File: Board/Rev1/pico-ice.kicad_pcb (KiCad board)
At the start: 4 copper layers, 22.9 x 61 mm, 99 parts, among them J1 USB_C_Receptacle_USB2.0, J2 Conn_02x20_Odd_Even, J3 Conn_02x20_Odd_Even, J4 PB_SEL, Q1 2N7002, SW1 PTS820 J25K SMTR LFS, SW2 PTS820 J25K SMTR LFS, U1 CL9293A12L5M, U2 W25Q32JVSSIQ, U3 RP2040, U4 CL9293A33L5M, U5 APS6404L-3SQN-SN, U6 ICE40UP5K-SG48ITR, U8 W25Q32JVSSIQ, Y1 12 MHz

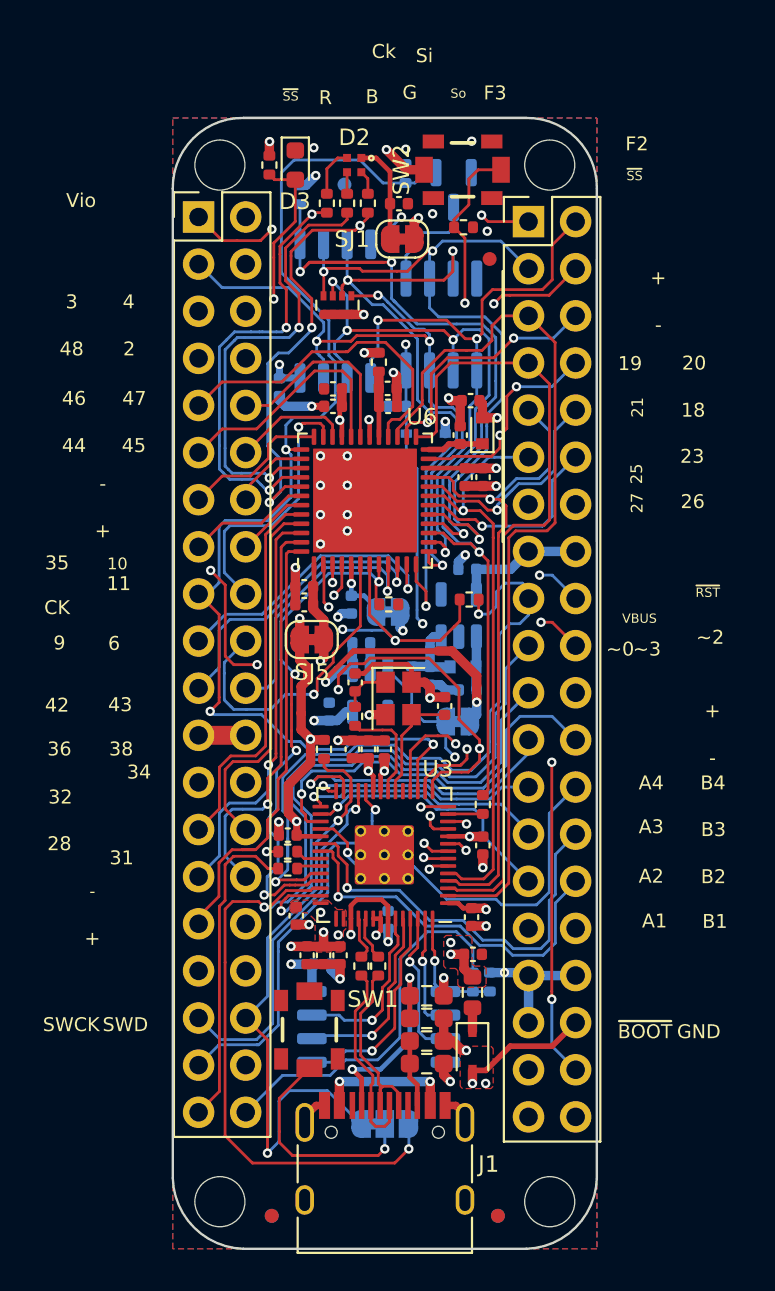
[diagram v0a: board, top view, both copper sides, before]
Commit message: Moved a few traces apart, esp on the clock related signals. Led to a couple of unwired signals.
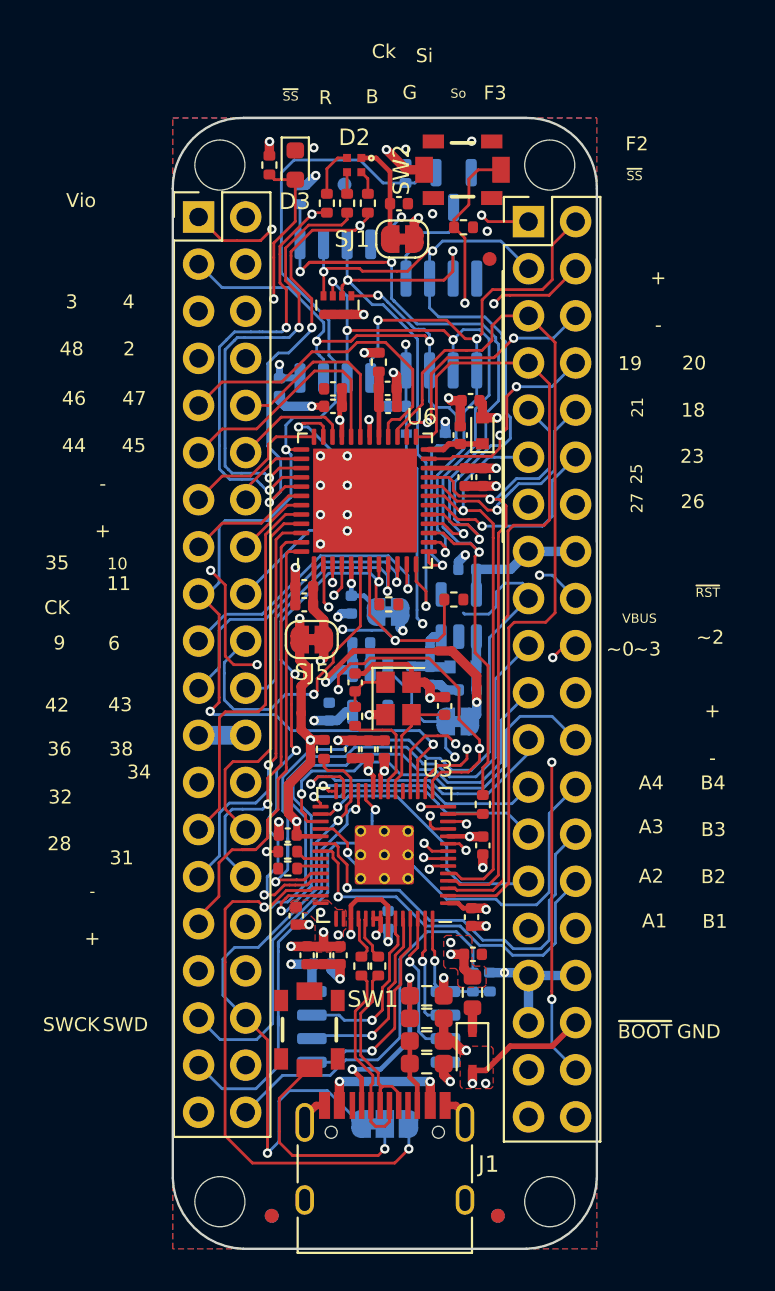
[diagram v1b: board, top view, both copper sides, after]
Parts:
- moved R25 0.83 mm to (76.1, 99.6)
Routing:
- net /SWCLK: track 21.3 -> 24.2 mm
- net /ICE_FLASH_IO2: track 45.5 -> 43.5 mm
- net /~{RESET}: track 33.6 -> 35.4 mm
- net /LED_R: track 73.3 -> 74.7 mm
- net /ICE_SI: track 60.1 -> 60.8 mm
- net /ICE_DONE_ADC0: track 37.4 -> 37.3 mm, vias 2 -> 1

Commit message: Update pico-ice.kicad_pcb
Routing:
- net /ICE_DONE_ADC0: track 37.3 -> 37.9 mm, vias 1 -> 2
- net /PICO_CLKOUT: track 16.9 -> 17.4 mm, vias 0 -> 1

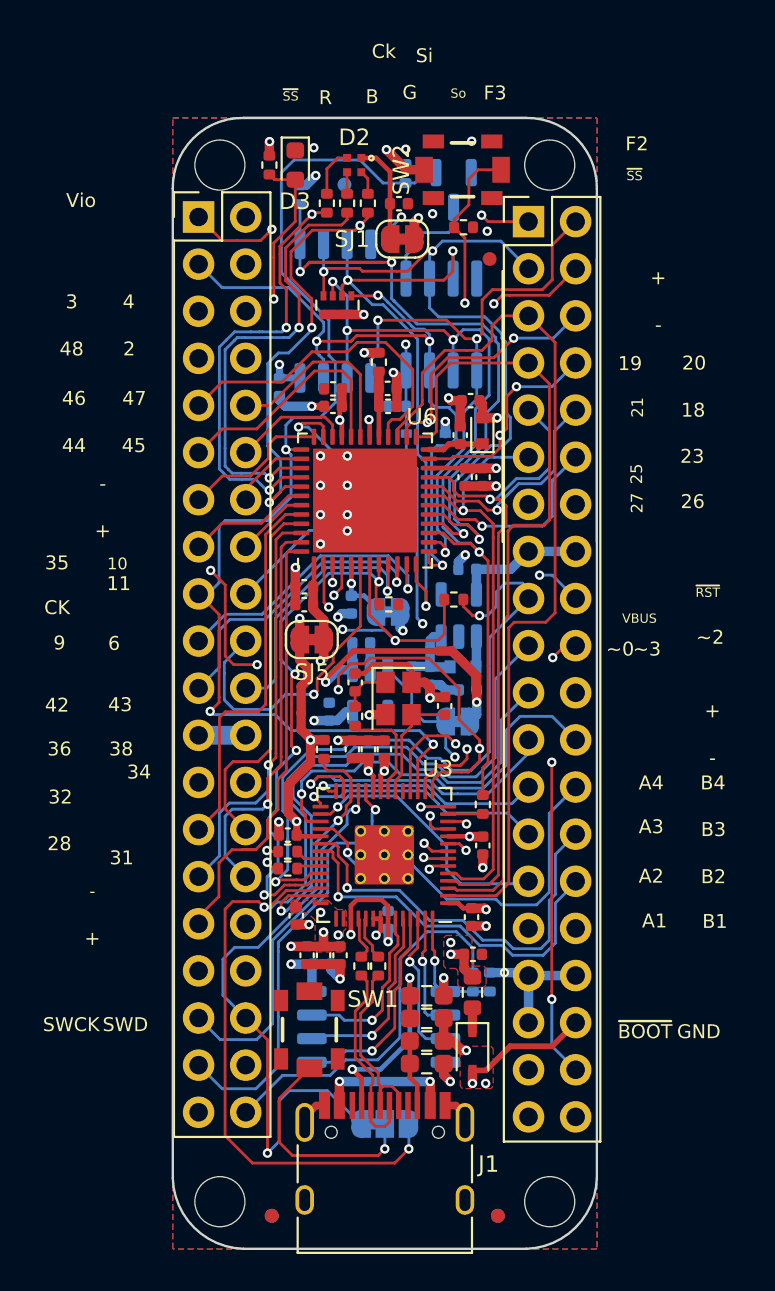
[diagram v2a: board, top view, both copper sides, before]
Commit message: Clean silkscreen
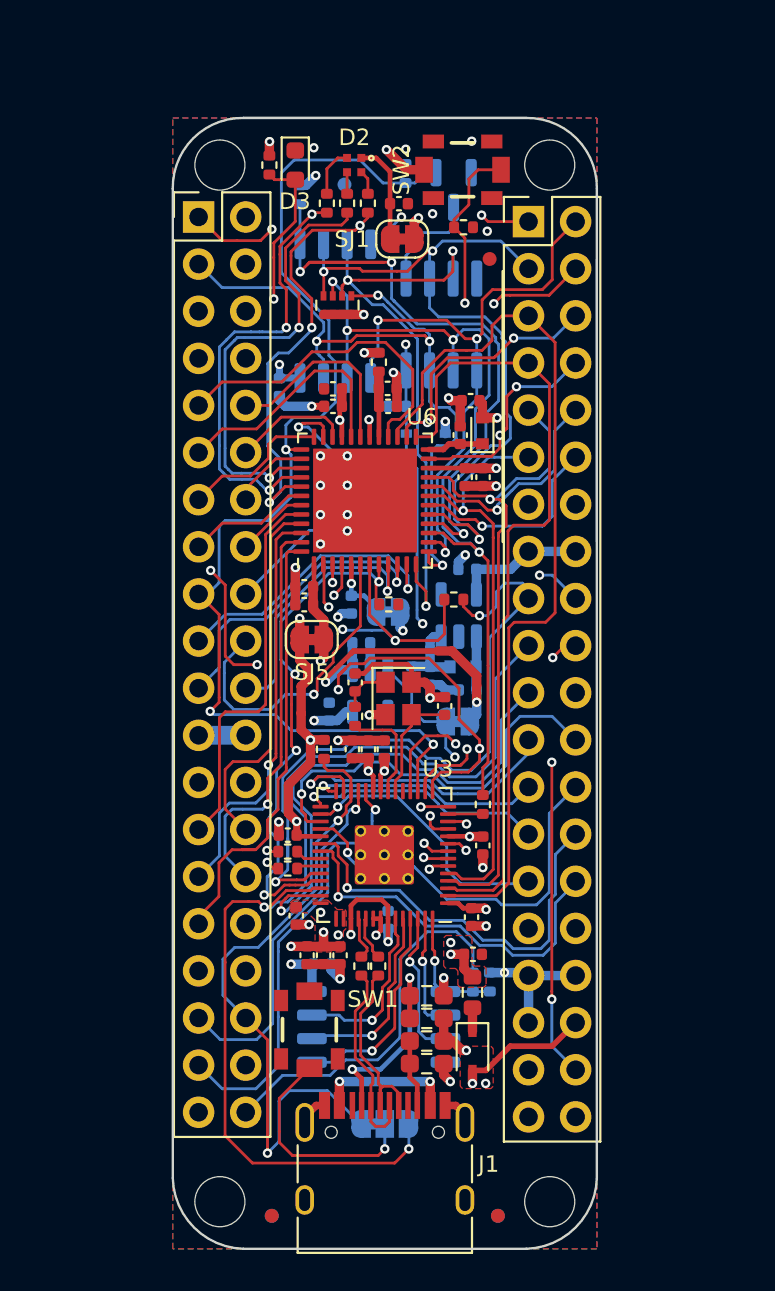
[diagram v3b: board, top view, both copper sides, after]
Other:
- board text removed: "+"
- board text removed: "-"
- board text removed: "10"
- board text removed: "11"
- board text removed: "18"
- board text removed: "19"
- board text removed: "2"
- board text removed: "20"
- board text removed: "21"
- board text removed: "23"
- board text removed: "25"
- board text removed: "26"
- board text removed: "27"
- board text removed: "28"
- board text removed: "3"
- board text removed: "31"
- board text removed: "32"
- board text removed: "34"
- board text removed: "35"
- board text removed: "36"
- board text removed: "38"
- board text removed: "4"
- board text removed: "42"
- board text removed: "43"
- board text removed: "44"
- board text removed: "45"
- board text removed: "46"
- board text removed: "47"
- board text removed: "48"
- board text removed: "6"
- board text removed: "9"
- board text removed: "A1"
- board text removed: "A2"
- board text removed: "A3"
- board text removed: "A4"
- board text removed: "B"
- board text removed: "B1"
- board text removed: "B2"
- board text removed: "B3"
- board text removed: "B4"
- board text removed: "CK"
- board text removed: "Ck"
- board text removed: "F2"
- board text removed: "F3"
- board text removed: "G"
- board text removed: "GND"
- board text removed: "R"
- board text removed: "RS"
- board text removed: "SWCK"
- board text removed: "SWD"
- board text removed: "Si"
- board text removed: "So"
- board text removed: "VBUS"
- board text removed: "Vio"
- board text removed: "~0"
- board text removed: "~2"
- board text removed: "~3"
- board text removed: "~{BOOT}"
- board text removed: "~{RST}"
- board text removed: "~{SS}"

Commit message: Update pico-ice.kicad_pcb
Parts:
- moved J2 1.02 mm to (62.2, 80.0)
- moved J3 0.77 mm to (80.0, 80.0)
- moved FID1 0.19 mm to (77.9, 81.3)
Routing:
- net /ICE_6: track 17.1 -> 12.6 mm
- net /ICE_4: track 29.8 -> 33.9 mm
- net /ICE_3: track 29.2 -> 33.2 mm
- net /LED_G: track 72.5 -> 70.0 mm
- net /PICO_PMOD_B3: track 22.2 -> 19.8 mm
- net /ICE_25: track 43.0 -> 41.0 mm
- net /~{ICE_RST}: track 53.2 -> 51.3 mm
- net /ICE_28: track 18.0 -> 19.7 mm
- net /ICE_35_G0: track 36.0 -> 37.6 mm
- net /LED_B: track 79.9 -> 78.2 mm
- net +3V3: track 60.3 -> 58.7 mm
- net /SRAM_SS: track 62.5 -> 64.1 mm
- net /ICE_27: track 48.2 -> 46.7 mm
- net /SWCLK: track 23.7 -> 22.3 mm
- net /ICE_SO: track 50.5 -> 49.2 mm
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
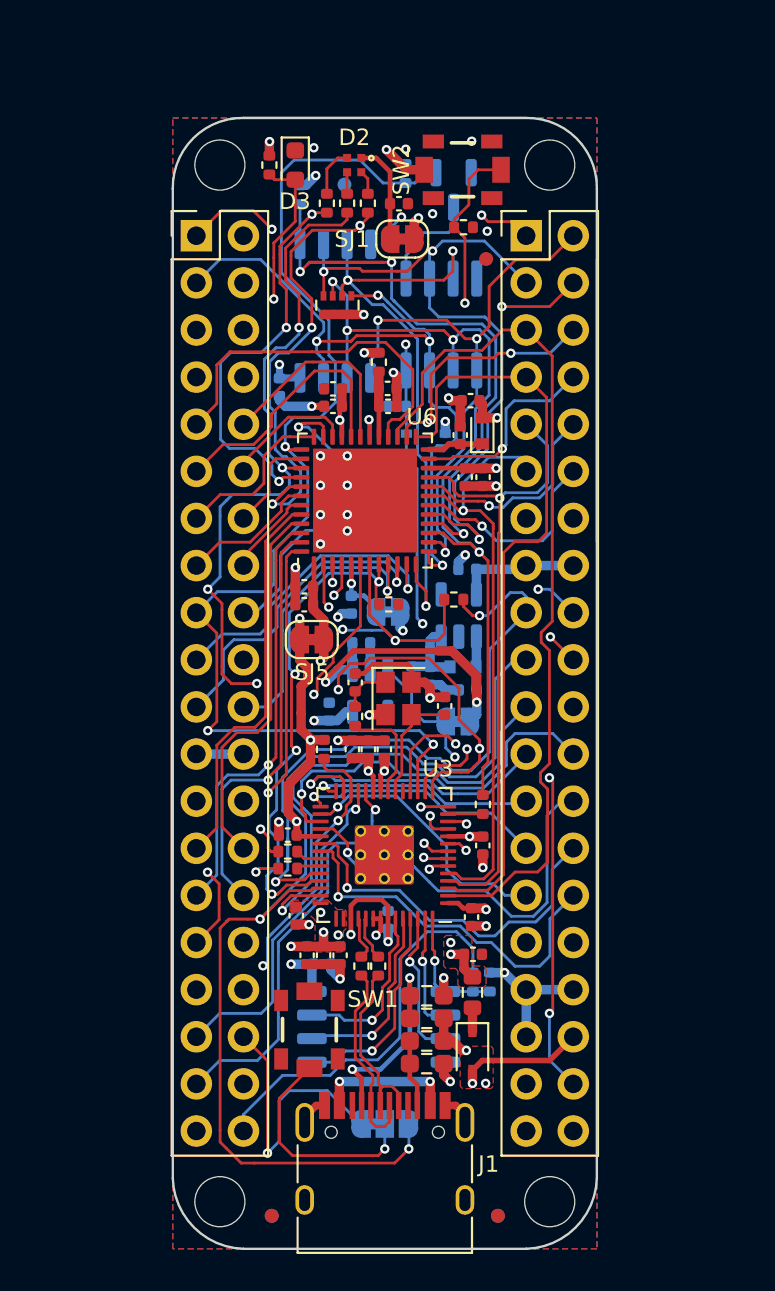
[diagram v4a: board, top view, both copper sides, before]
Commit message: Added silkscreen details, minor routing change to clear the logo
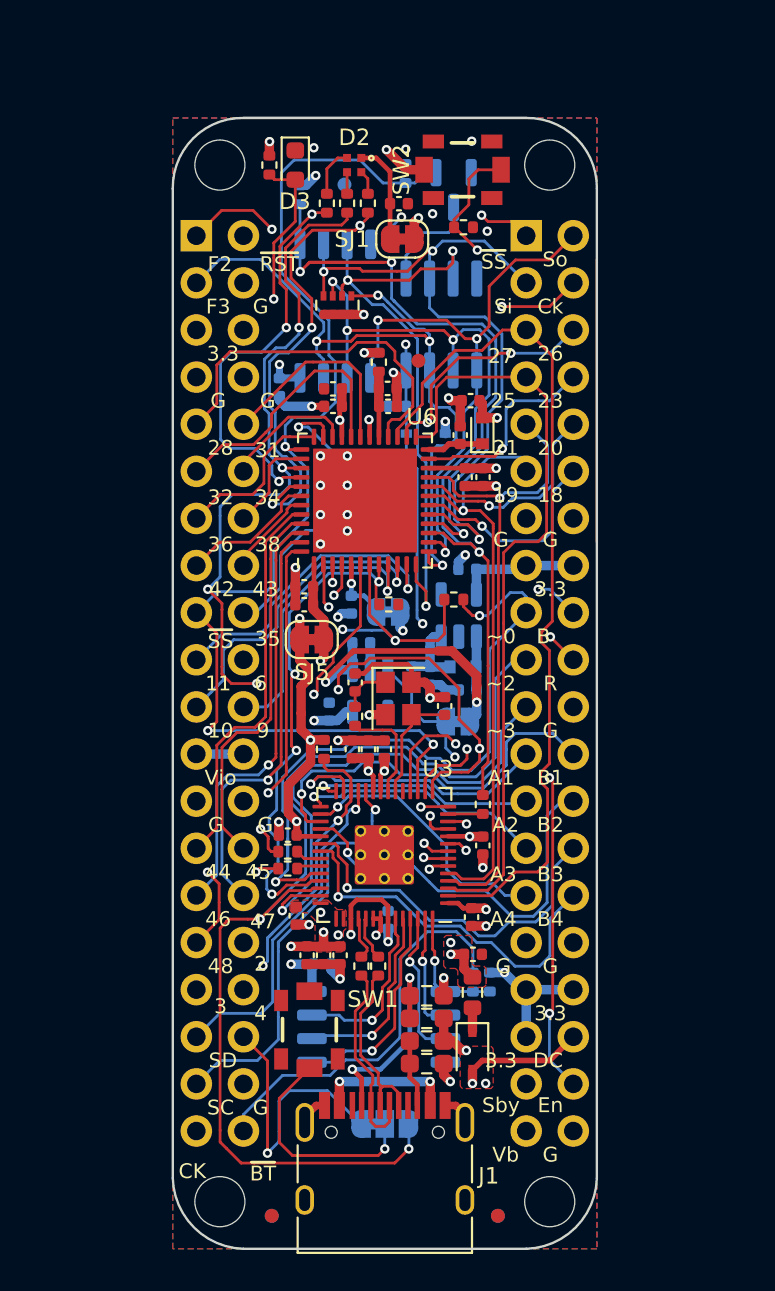
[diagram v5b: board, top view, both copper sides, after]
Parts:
- moved FID1 6.59 mm to (74.2, 86.7)
- moved LOGO3 1.48 mm to (71.2, 95.3)
- moved LOGO1 0.84 mm to (75.0, 83.2)
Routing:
- net /ICE_10|PB: track 43.1 -> 43.7 mm
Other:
- board text added: "10"
- board text added: "11"
- board text added: "18"
- board text added: "19"
- board text added: "2"
- board text added: "20"
- board text added: "21"
- board text added: "23"
- board text added: "25"
- board text added: "26"
- board text added: "27"
- board text added: "28"
- board text added: "3"
- board text added: "3.3"
- board text added: "31"
- board text added: "32"
- board text added: "34"
- board text added: "35"
- board text added: "36"
- board text added: "38"
- board text added: "4"
- board text added: "42"
- board text added: "43"
- board text added: "44"
- board text added: "45"
- board text added: "46"
- board text added: "47"
- board text added: "48"
- board text added: "6"
- board text added: "9"
- board text added: "A1"
- board text added: "A2"
- board text added: "A3"
- board text added: "A4"
- board text added: "B"
- board text added: "B1"
- board text added: "B2"
- board text added: "B3"
- board text added: "B4"
- board text added: "CK"
- board text added: "Ck"
- board text added: "DC"
- board text added: "En"
- board text added: "F2"
- board text added: "F3"
- board text added: "G"
- board text added: "R"
- board text added: "SC"
- board text added: "SD"
- board text added: "Sby"
- board text added: "Si"
- board text added: "So"
- board text added: "Vb"
- board text added: "Vbus"
- board text added: "Vio"
- board text added: "pico-ice v2"
- board text added: "~0"
- board text added: "~2"
- board text added: "~3"
- board text added: "~{BT}"
- board text added: "~{RST}"
- board text added: "~{Rst}"
- board text added: "~{SS}"
